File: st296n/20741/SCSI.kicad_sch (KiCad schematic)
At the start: 23 parts, among them J8 SCSI, Q13 BC846A, U11 11734-501, U3 74LS14, U30 74F08, U5 AIC-010L, U7 SRAM_6116

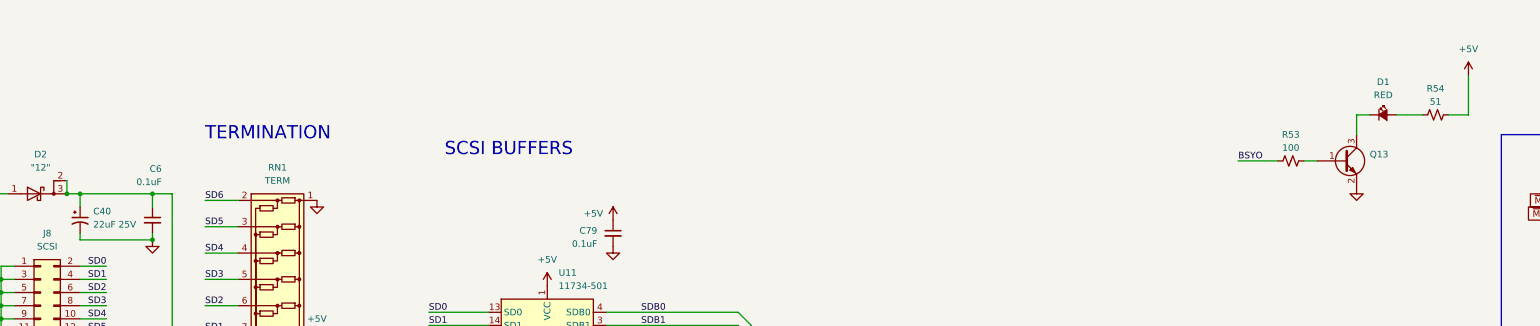
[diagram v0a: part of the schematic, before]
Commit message: st296n fix passives
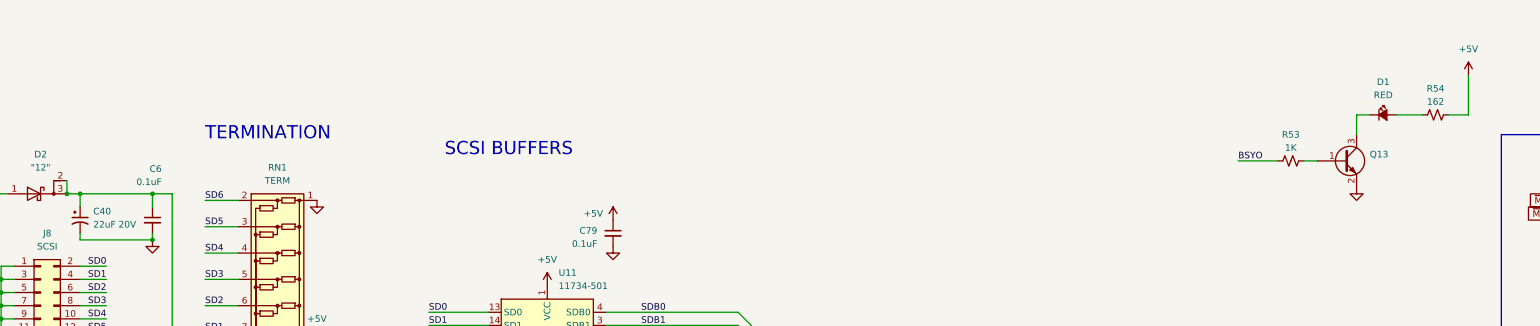
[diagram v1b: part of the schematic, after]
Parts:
- C40: value 22uF 25V -> 22uF 20V
- R53: value 100 -> 1K
- R54: value 51 -> 162
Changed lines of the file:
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@@
 			)
 		)
-		(property "Value" "100"
+		(property "Value" "1K"
 			(at 278.13 81.28 90)
 			(effects
@@
 		(dnp no)
 		(fields_autoplaced yes)
-		(property "Reference" "#PWR02"
+		(property "Reference" "#PWR078"
 			(at 90.17 123.19 0)
 			(effects
@@
 			)
 		)
-		(property "Value" "51"
+		(property "Value" "162"
 			(at 306.07 72.39 90)
 			(effects
@@
 		(dnp no)
 		(fields_autoplaced yes)
-		(property "Reference" "#PWR01"
+		(property "Reference" "#PWR0101"
 			(at 90.17 171.45 0)
 			(effects
@@
 		(dnp no)
 		(fields_autoplaced yes)
-		(property "Reference" "#PWR01"
+		(property "Reference" "#PWR084"
 			(at 358.14 115.57 0)
 			(effects
@@
 		(on_board yes)
 		(dnp no)
-		(property "Reference" "#PWR02"
+		(property "Reference" "#PWR034"
 			(at 359.41 165.1 0)
 			(effects
@@
 		(dnp no)
 		(fields_autoplaced yes)
-		(property "Reference" "#PWR01"
+		(property "Reference" "#PWR094"
 			(at 90.17 134.62 0)
 			(effects
@@
 		(dnp no)
 		(fields_autoplaced yes)
-		(property "Reference" "#PWR01"
+		(property "Reference" "#PWR0116"
 			(at 374.65 223.52 0)
 			(effects
@@
 		(dnp no)
 		(fields_autoplaced yes)
-		(property "Reference" "#PWR01"
+		(property "Reference" "#PWR0103"
 			(at 228.6 220.98 0)
 			(effects
@@
 		(dnp no)
 		(fields_autoplaced yes)
-		(property "Reference" "#PWR02"
+		(property "Reference" "#PWR069"
 			(at 228.6 172.72 0)
 			(effects
@@
 		(dnp no)
 		(fields_autoplaced yes)
-		(property "Reference" "#PWR02"
+		(property "Reference" "#PWR063"
 			(at 358.14 41.91 0)
 			(effects
@@
 		(dnp no)
 		(fields_autoplaced yes)
-		(property "Reference" "#PWR01"
+		(property "Reference" "#PWR089"
 			(at 90.17 97.79 0)
 			(effects
@@
 		(dnp no)
 		(fields_autoplaced yes)
-		(property "Reference" "#PWR02"
+		(property "Reference" "#PWR076"
 			(at 90.17 160.02 0)
 			(effects
@@
 		(dnp no)
 		(fields_autoplaced yes)
-		(property "Reference" "#PWR02"
+		(property "Reference" "#PWR0106"
 			(at 312.42 71.12 0)
 			(effects
@@
 		(dnp no)
 		(fields_autoplaced yes)
-		(property "Reference" "#PWR01"
+		(property "Reference" "#PWR035"
 			(at 359.41 237.49 0)
 			(effects
@@
 		(fields_autoplaced yes)
 		(property "Reference" "C40"
-			(at 46.99 93.5482 0)
+			(at 46.99 93.5481 0)
 			(effects
 				(font
@@
 			)
 		)
-		(property "Value" "22uF 25V"
-			(at 46.99 96.0882 0)
+		(property "Value" "22uF 20V"
+			(at 46.99 96.0881 0)
 			(effects
 				(font
@@
 		(dnp no)
 		(fields_autoplaced yes)
-		(property "Reference" "#PWR02"
+		(property "Reference" "#PWR082"
 			(at 90.17 196.85 0)
 			(effects

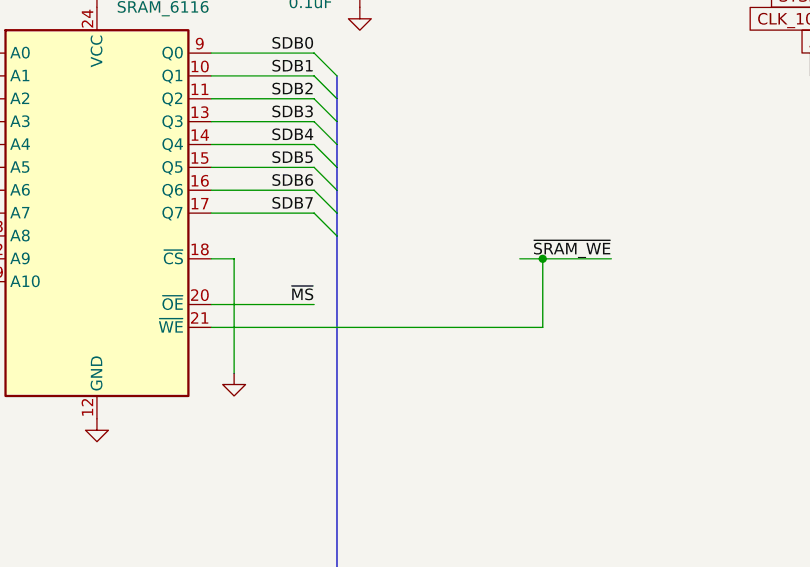
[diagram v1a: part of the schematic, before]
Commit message: Add ST-251N. Update ST-296N to show changes.
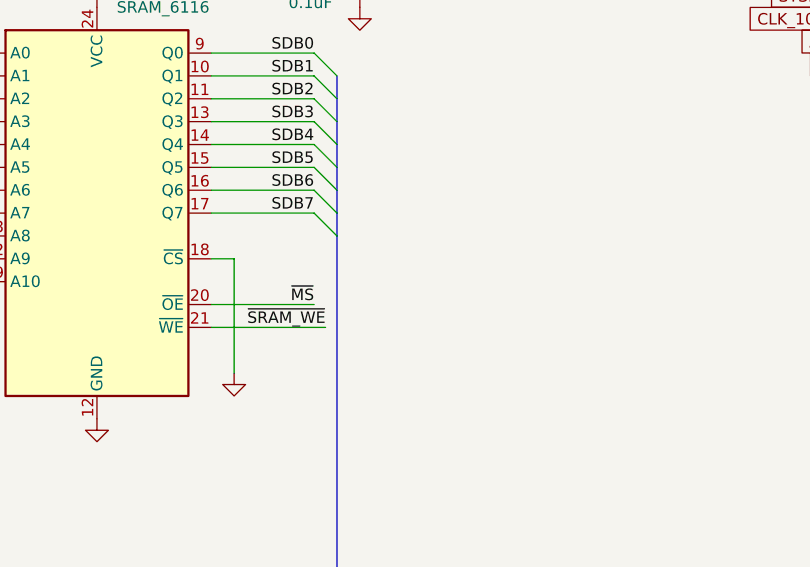
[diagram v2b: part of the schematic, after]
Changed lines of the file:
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@@
 	)
 	(junction
-		(at 278.13 196.85)
-		(diameter 0)
-		(color 0 0 0 0)
-	)
-	(junction
 		(at 29.21 124.46)
 		(diameter 0)
@@
 		)
 	)
-	(wire
-		(pts
-			(xy 275.59 196.85) (xy 278.13 196.85)
-		)
-		(stroke
-			(width 0)
-			(type default)
-		)
-	)
 	(bus
 		(pts
@@
 	(wire
 		(pts
-			(xy 278.13 204.47) (xy 278.13 196.85)
-		)
-		(stroke
-			(width 0)
-			(type default)
-		)
-	)
-	(wire
-		(pts
 			(xy 373.38 187.96) (xy 384.81 187.96)
 		)
@@
 		)
 	)
-	(wire
-		(pts
-			(xy 278.13 196.85) (xy 285.75 196.85)
-		)
-		(stroke
-			(width 0)
-			(type default)
-		)
-	)
 	(bus
 		(pts
@@
 	(wire
 		(pts
-			(xy 241.3 204.47) (xy 278.13 204.47)
+			(xy 241.3 204.47) (xy 254 204.47)
 		)
 		(stroke
@@
 			(font
 				(size 1.27 1.27)
+				(color 255 0 255 1)
 			)
 			(justify left bottom)
@@
 	)
 	(label "~{SRAM_WE}"
-		(at 285.75 196.85 180)
+		(at 254 204.47 180)
 		(fields_autoplaced yes)
 		(effects
@@
 			(font
 				(size 1.27 1.27)
+				(color 255 0 255 1)
 			)
 			(justify left bottom)
